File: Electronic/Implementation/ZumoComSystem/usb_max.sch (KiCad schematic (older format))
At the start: 8 parts, among them J1 USB_A_Molex_105057, U3 MAX3421EEHJ+T, Y1 FL1200112_12MHz

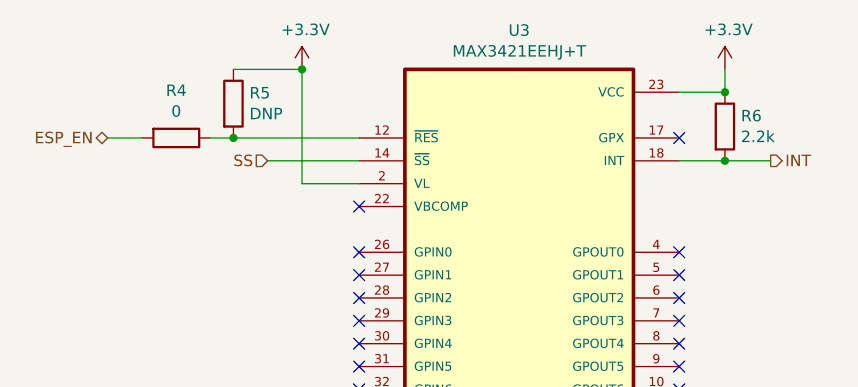
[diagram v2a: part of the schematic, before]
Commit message: #93 ESP32 3V3 Diode; U_Bat_Meas from Pin IO2 to IO13; Test-Vias D+,D-
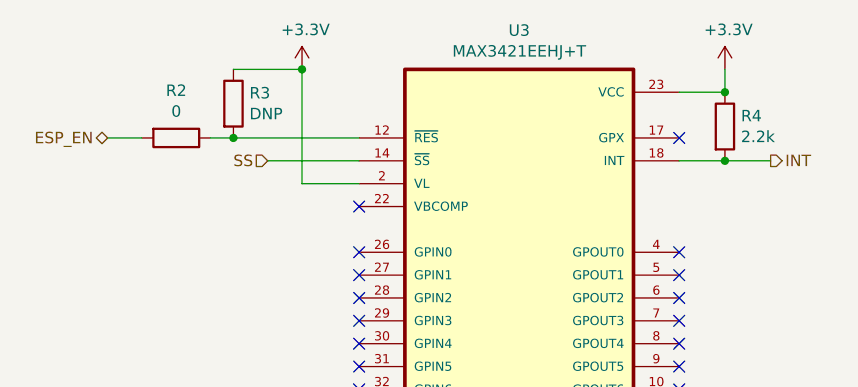
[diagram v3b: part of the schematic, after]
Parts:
- renumbered R4 to R2, R5 to R3, R6 to R4
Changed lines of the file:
@@
 	4650 2150 4400 2150
 $Comp
-L Device:R R6
+L Device:R R4
 U 1 1 6256E0B6
 P 6250 1900
-F 0 "R6" H 6320 1946 50  0000 L CNN
+F 0 "R4" H 6320 1946 50  0000 L CNN
 F 1 "2.2k" H 6320 1855 50  0000 L CNN
 F 2 "Resistor_SMD:R_0603_1608Metric_Pad1.05x0.95mm_HandSolder" V 6180 1900 50  0001 C CNN
@@
 	4650 1950 4100 1950
 $Comp
-L Device:R R5
+L Device:R R3
 U 1 1 6256E70A
 P 4100 1800
-F 0 "R5" H 4170 1846 50  0000 L CNN
+F 0 "R3" H 4170 1846 50  0000 L CNN
 F 1 "DNP" H 4170 1755 50  0000 L CNN
 F 2 "Resistor_SMD:R_0603_1608Metric_Pad1.05x0.95mm_HandSolder" V 4030 1800 50  0001 C CNN
@@
 Connection ~ 4400 1650
 $Comp
-L Device:R R4
+L Device:R R2
 U 1 1 62574913
 P 3850 1950
-F 0 "R4" V 3643 1950 50  0000 C CNN
+F 0 "R2" V 3643 1950 50  0000 C CNN
 F 1 "0" V 3734 1950 50  0000 C CNN
 F 2 "Resistor_SMD:R_0603_1608Metric_Pad1.05x0.95mm_HandSolder" V 3780 1950 50  0001 C CNN

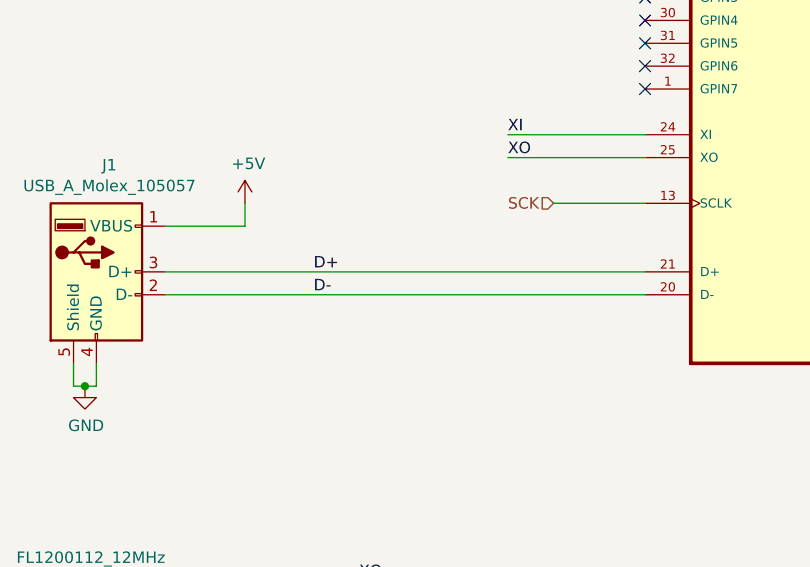
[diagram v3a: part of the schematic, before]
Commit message: #93 USB-Max TestVias (D+,D-); Serial Resistors (22 Ohm)
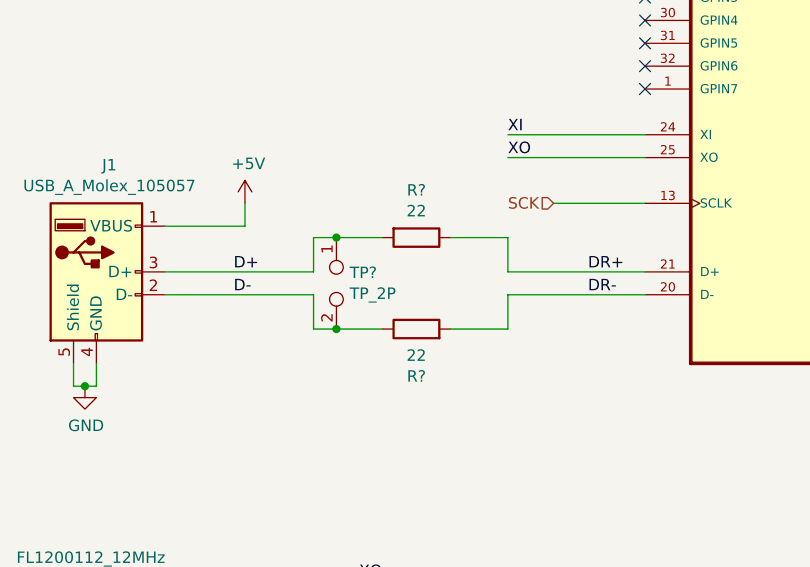
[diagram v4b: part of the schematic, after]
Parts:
- added R? (x2): 22, Resistor_SMD:R_0603_1608Metric_Pad1.05x0.95mm_HandSolder, symbol Device:R
- added TP?: TP_2P, Connector_PinHeader_2.54mm:PinHeader_1x02_P2.54mm_Vertical, symbol Connector:TestPoint_2Pole
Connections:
- net D+: now also R?.2, TP?.1; no longer U3.21 (D+)
- net D-: now also R?.1, TP?.2; no longer U3.20 (D-)
- new net DR+: R?.1, U3.21 (D+)
- new net DR-: R?.2, U3.20 (D-)
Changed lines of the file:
@@
 	6050 3750 6450 3750
-Wire Wire Line
-	2550 3950 4650 3950
-Wire Wire Line
-	2550 4050 4650 4050
 Wire Wire Line
 	2250 4350 2250 4450
@@
 	3000 5400 3500 5400
 Connection ~ 3000 5950
-Text Label 3200 3950 0    50   ~ 0
+Text Label 2850 3950 0    50   ~ 0
 D+
-Text Label 3200 4050 0    50   ~ 0
+Text Label 2850 4050 0    50   ~ 0
 D-
 Text Label 4050 3350 0    50   ~ 0
@@
 Wire Wire Line
 	4000 1950 4100 1950
+$Comp
+L Connector:TestPoint_2Pole TP?
+U 1 1 62EEE2C4
+P 3300 4000
+AR Path="/60C4E4D0/62EEE2C4" Ref="TP?"  Part="1"
+AR Path="/60C500E6/62EEE2C4" Ref="TP?"  Part="1"
+F 0 "TP?" V 3254 4058 50  0000 L CNN
+F 1 "TP_2P" V 3345 4058 50  0000 L CNN
+F 2 "Connector_PinHeader_2.54mm:PinHeader_1x02_P2.54mm_Vertical" H 3300 4000 50  0001 C CNN
+F 3 "~" H 3300 4000 50  0001 C CNN
+	1    3300 4000
+	0    1    1    0
+$EndComp
+Wire Wire Line
+	2550 3950 3200 3950
+Wire Wire Line
+	3200 3800 3300 3800
+Wire Wire Line
+	4050 3800 4050 3950
+Wire Wire Line
+	4050 3950 4650 3950
+Connection ~ 3300 3800
+Wire Wire Line
+	3300 3800 3500 3800
+Wire Wire Line
+	3200 3800 3200 3950
+Wire Wire Line
+	2550 4050 3200 4050
+Wire Wire Line
+	3200 4200 3300 4200
+Wire Wire Line
+	4050 4200 4050 4050
+Wire Wire Line
+	4050 4050 4650 4050
+Wire Wire Line
+	4050 4200 3800 4200
+Connection ~ 3300 4200
+Wire Wire Line
+	3200 4050 3200 4200
+Text Label 4400 3950 0    50   ~ 0
+DR+
+Text Label 4400 4050 0    50   ~ 0
+DR-
+$Comp
+L Device:R R?
+U 1 1 62EF4C70
+P 3650 3800
+F 0 "R?" V 3443 3800 50  0000 C CNN
+F 1 "22" V 3534 3800 50  0000 C CNN
+F 2 "Resistor_SMD:R_0603_1608Metric_Pad1.05x0.95mm_HandSolder" V 3580 3800 50  0001 C CNN
+F 3 "~" H 3650 3800 50  0001 C CNN
+F 4 "" H 3650 3800 50  0001 C CNN "Manufacturer"
+F 5 "" H 3650 3800 50  0001 C CNN "Part-No."
+	1    3650 3800
+	0    1    1    0
+$EndComp
+Wire Wire Line
+	3800 3800 4050 3800
+$Comp
+L Device:R R?
+U 1 1 62EF55BF
+P 3650 4200
+F 0 "R?" V 3443 4200 50  0000 C CNN
+F 1 "22" V 3534 4200 50  0000 C CNN
+F 2 "Resistor_SMD:R_0603_1608Metric_Pad1.05x0.95mm_HandSolder" V 3580 4200 50  0001 C CNN
+F 3 "~" H 3650 4200 50  0001 C CNN
+F 4 "" H 3650 4200 50  0001 C CNN "Manufacturer"
+F 5 "" H 3650 4200 50  0001 C CNN "Part-No."
+	1    3650 4200
+	0    -1   -1   0
+$EndComp
+Wire Wire Line
+	3500 4200 3300 4200
 $EndSCHEMATC

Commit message: Annotation update annotation
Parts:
- gave numbers to parts that had none: 3
- renumbered R2 to R4, R3 to R5, R4 to R6
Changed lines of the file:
@@
 	4650 2150 4400 2150
 $Comp
-L Device:R R4
+L Device:R R6
 U 1 1 6256E0B6
 P 6250 1900
-F 0 "R4" H 6320 1946 50  0000 L CNN
+F 0 "R6" H 6320 1946 50  0000 L CNN
 F 1 "2.2k" H 6320 1855 50  0000 L CNN
 F 2 "Resistor_SMD:R_0603_1608Metric_Pad1.05x0.95mm_HandSolder" V 6180 1900 50  0001 C CNN
@@
 	4650 1950 4100 1950
 $Comp
-L Device:R R3
+L Device:R R5
 U 1 1 6256E70A
 P 4100 1800
-F 0 "R3" H 4170 1846 50  0000 L CNN
+F 0 "R5" H 4170 1846 50  0000 L CNN
 F 1 "DNP" H 4170 1755 50  0000 L CNN
 F 2 "Resistor_SMD:R_0603_1608Metric_Pad1.05x0.95mm_HandSolder" V 4030 1800 50  0001 C CNN
@@
 Connection ~ 4400 1650
 $Comp
-L Device:R R2
+L Device:R R4
 U 1 1 62574913
 P 3850 1950
-F 0 "R2" V 3643 1950 50  0000 C CNN
+F 0 "R4" V 3643 1950 50  0000 C CNN
 F 1 "0" V 3734 1950 50  0000 C CNN
 F 2 "Resistor_SMD:R_0603_1608Metric_Pad1.05x0.95mm_HandSolder" V 3780 1950 50  0001 C CNN
@@
 P 3300 4000
 AR Path="/60C4E4D0/62EEE2C4" Ref="TP?"  Part="1"
-AR Path="/60C500E6/62EEE2C4" Ref="TP?"  Part="1"
-F 0 "TP?" V 3254 4058 50  0000 L CNN
+AR Path="/60C500E6/62EEE2C4" Ref="TP1"  Part="1"
+F 0 "TP1" V 3254 4058 50  0000 L CNN
 F 1 "TP_2P" V 3345 4058 50  0000 L CNN
 F 2 "Connector_PinHeader_2.54mm:PinHeader_1x02_P2.54mm_Vertical" H 3300 4000 50  0001 C CNN
@@
 DR-
 $Comp
-L Device:R R?
+L Device:R R2
 U 1 1 62EF4C70
 P 3650 3800
-F 0 "R?" V 3443 3800 50  0000 C CNN
+F 0 "R2" V 3443 3800 50  0000 C CNN
 F 1 "22" V 3534 3800 50  0000 C CNN
 F 2 "Resistor_SMD:R_0603_1608Metric_Pad1.05x0.95mm_HandSolder" V 3580 3800 50  0001 C CNN
@@
 	3800 3800 4050 3800
 $Comp
-L Device:R R?
+L Device:R R3
 U 1 1 62EF55BF
 P 3650 4200
-F 0 "R?" V 3443 4200 50  0000 C CNN
+F 0 "R3" V 3443 4200 50  0000 C CNN
 F 1 "22" V 3534 4200 50  0000 C CNN
 F 2 "Resistor_SMD:R_0603_1608Metric_Pad1.05x0.95mm_HandSolder" V 3580 4200 50  0001 C CNN

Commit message: #93 small fixes
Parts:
- R2, R3: Manufacturer (none) -> YAGEO; Part-No. (none) -> RC0603JR-1322RL
- TP1: Manufacturer (none) -> -; Part-No. (none) -> -
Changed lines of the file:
@@
 Sheet 3 7
 Title "Zumo Communication System"
-Date "2022-08-04"
+Date "2022-08-05"
 Rev "V1.1"
 Comp "NewTec GmbH"
@@
 F 2 "Connector_PinHeader_2.54mm:PinHeader_1x02_P2.54mm_Vertical" H 3300 4000 50  0001 C CNN
 F 3 "~" H 3300 4000 50  0001 C CNN
+F 4 "-" H 3300 4000 50  0001 C CNN "Manufacturer"
+F 5 "-" H 3300 4000 50  0001 C CNN "Part-No."
 	1    3300 4000
 	0    1    1    0
@@
 F 2 "Resistor_SMD:R_0603_1608Metric_Pad1.05x0.95mm_HandSolder" V 3580 3800 50  0001 C CNN
 F 3 "~" H 3650 3800 50  0001 C CNN
-F 4 "" H 3650 3800 50  0001 C CNN "Manufacturer"
-F 5 "" H 3650 3800 50  0001 C CNN "Part-No."
+F 4 "YAGEO" H 3650 3800 50  0001 C CNN "Manufacturer"
+F 5 "RC0603JR-1322RL " H 3650 3800 50  0001 C CNN "Part-No."
 	1    3650 3800
 	0    1    1    0
@@
 F 2 "Resistor_SMD:R_0603_1608Metric_Pad1.05x0.95mm_HandSolder" V 3580 4200 50  0001 C CNN
 F 3 "~" H 3650 4200 50  0001 C CNN
-F 4 "" H 3650 4200 50  0001 C CNN "Manufacturer"
-F 5 "" H 3650 4200 50  0001 C CNN "Part-No."
+F 4 "YAGEO" H 3650 4200 50  0001 C CNN "Manufacturer"
+F 5 "RC0603JR-1322RL " H 3650 4200 50  0001 C CNN "Part-No."
 	1    3650 4200
 	0    -1   -1   0
